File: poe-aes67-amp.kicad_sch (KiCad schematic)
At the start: 0 parts

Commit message: Setting up KiCad
Add symbols and footprints for Sheet 2 components
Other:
- added sheet Amp_Stage (sheets/amp_stage.kicad_sch)
- added sheet CM4_Carrier (sheets/cm4_carrier.kicad_sch)
- added sheet IO_Misc (sheets/io_misc.kicad_sch)
- added sheet PoE_PD (sheets/poe_pd.kicad_sch .kicad_sch)
- added sheet Power_Rails (sheets/power_rails.kicad_sch)
- company: (none) -> JCJOK3R
- title: (none) -> PoE AES67 Amplifier
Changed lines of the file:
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@@
 	(generator_version "10.0")
 	(paper "A4")
+	(title_block
+		(title "PoE AES67 Amplifier")
+		(date "2026-06-03")
+		(rev "0.1")
+		(company "JCJOK3R")
+		(comment 1 "CERN-OHL-S v2")
+	)
+	(sheet
+		(at 73.66 26.67)
+		(size 40.64 24.13)
+		(exclude_from_sim no)
+		(in_bom yes)
+		(on_board yes)
+		(dnp no)
+		(fields_autoplaced yes)
+		(stroke
+			(width 0.1524)
+			(type solid)
+		)
+		(fill
+			(color 0 0 0 0)
+		)
+		(property "Sheetname" "Power_Rails"
+			(at 73.66 25.9584 0)
+			(show_name no)
+			(do_not_autoplace no)
+			(effects
+				(font
+					(size 1.27 1.27)
+				)
+				(justify left bottom)
+			)
+		)
+		(property "Sheetfile" "sheets/power_rails.kicad_sch"
+			(at 73.66 51.3846 0)
+			(show_name no)
+			(do_not_autoplace no)
+			(effects
+				(font
+					(size 1.27 1.27)
+				)
+				(justify left top)
+			)
+		)
+		(instances
+			(project "poe-aes67-amp"
+				(path "/342711d1-e6c4-426d-85fd-6094774cf2a5"
+					(page "3")
+				)
+			)
+		)
+	)
+	(sheet
+		(at 124.46 76.2)
+		(size 38.1 24.13)
+		(exclude_from_sim no)
+		(in_bom yes)
+		(on_board yes)
+		(dnp no)
+		(fields_autoplaced yes)
+		(stroke
+			(width 0.1524)
+			(type solid)
+		)
+		(fill
+			(color 0 0 0 0)
+		)
+		(property "Sheetname" "CM4_Carrier"
+			(at 124.46 75.4884 0)
+			(show_name no)
+			(do_not_autoplace no)
+			(effects
+				(font
+					(size 1.27 1.27)
+				)
+				(justify left bottom)
+			)
+		)
+		(property "Sheetfile" "sheets/cm4_carrier.kicad_sch"
+			(at 124.46 100.9146 0)
+			(show_name no)
+			(do_not_autoplace no)
+			(effects
+				(font
+					(size 1.27 1.27)
+				)
+				(justify left top)
+			)
+		)
+		(instances
+			(project "poe-aes67-amp"
+				(path "/342711d1-e6c4-426d-85fd-6094774cf2a5"
+					(page "5")
+				)
+			)
+		)
+	)
+	(sheet
+		(at 173.99 76.2)
+		(size 34.29 24.13)
+		(exclude_from_sim no)
+		(in_bom yes)
+		(on_board yes)
+		(dnp no)
+		(fields_autoplaced yes)
+		(stroke
+			(width 0.1524)
+			(type solid)
+		)
+		(fill
+			(color 0 0 0 0)
+		)
+		(property "Sheetname" "IO_Misc"
+			(at 173.99 75.4884 0)
+			(show_name no)
+			(do_not_autoplace no)
+			(effects
+				(font
+					(size 1.27 1.27)
+				)
+				(justify left bottom)
+			)
+		)
+		(property "Sheetfile" "sheets/io_misc.kicad_sch"
+			(at 173.99 100.9146 0)
+			(show_name no)
+			(do_not_autoplace no)
+			(effects
+				(font
+					(size 1.27 1.27)
+				)
+				(justify left top)
+			)
+		)
+		(instances
+			(project "poe-aes67-amp"
+				(path "/342711d1-e6c4-426d-85fd-6094774cf2a5"
+					(page "6")
+				)
+			)
+		)
+	)
+	(sheet
+		(at 20.32 25.4)
+		(size 41.91 25.4)
+		(exclude_from_sim no)
+		(in_bom yes)
+		(on_board yes)
+		(dnp no)
+		(fields_autoplaced yes)
+		(stroke
+			(width 0.1524)
+			(type solid)
+		)
+		(fill
+			(color 0 0 0 0)
+		)
+		(property "Sheetname" "PoE_PD"
+			(at 20.32 24.6884 0)
+			(show_name no)
+			(do_not_autoplace no)
+			(effects
+				(font
+					(size 1.27 1.27)
+				)
+				(justify left bottom)
+			)
+		)
+		(property "Sheetfile" "sheets/poe_pd.kicad_sch .kicad_sch"
+			(at 20.32 51.3846 0)
+			(show_name no)
+			(do_not_autoplace no)
+			(effects
+				(font
+					(size 1.27 1.27)
+				)
+				(justify left top)
+			)
+		)
+		(instances
+			(project "poe-aes67-amp"
+				(path "/342711d1-e6c4-426d-85fd-6094774cf2a5"
+					(page "2")
+				)
+			)
+		)
+	)
+	(sheet
+		(at 124.46 27.94)
+		(size 38.1 22.86)
+		(exclude_from_sim no)
+		(in_bom yes)
+		(on_board yes)
+		(dnp no)
+		(fields_autoplaced yes)
+		(stroke
+			(width 0.1524)
+			(type solid)
+		)
+		(fill
+			(color 0 0 0 0)
+		)
+		(property "Sheetname" "Amp_Stage"
+			(at 124.46 27.2284 0)
+			(show_name no)
+			(do_not_autoplace no)
+			(effects
+				(font
+					(size 1.27 1.27)
+				)
+				(justify left bottom)
+			)
+		)
+		(property "Sheetfile" "sheets/amp_stage.kicad_sch"
+			(at 124.46 51.3846 0)
+			(show_name no)
+			(do_not_autoplace no)
+			(effects
+				(font
+					(size 1.27 1.27)
+				)
+				(justify left top)
+			)
+		)
+		(instances
+			(project "poe-aes67-amp"
+				(path "/342711d1-e6c4-426d-85fd-6094774cf2a5"
+					(page "4")
+				)
+			)
+		)
+	)
 	(sheet_instances
 		(path "/"

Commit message: Buck A config
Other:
- sheet PoE_PD ports: added BUCK_A_EN, LED_ACT, MDI1_N, MDI1_P, MDI2_N, MDI2_P, MDI3_N, MDI3_P, MDI4_N, MDI4_P; removed none
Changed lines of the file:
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@@
+			)
+		)
+		(pin "BUCK_A_EN" output
+			(at 59.69 50.8 270)
+			(effects
+				(font
+					(size 1.27 1.27)
+				)
+				(justify left)
+			)
+		)
+		(pin "LED_ACT" output
+			(at 57.15 50.8 270)
+			(effects
+				(font
+					(size 1.27 1.27)
+				)
+				(justify left)
+			)
+		)
+		(pin "MDI1_N" output
+			(at 54.61 50.8 270)
+			(effects
+				(font
+					(size 1.27 1.27)
+				)
+				(justify left)
+			)
+		)
+		(pin "MDI1_P" output
+			(at 52.07 50.8 270)
+			(effects
+				(font
+					(size 1.27 1.27)
+				)
+				(justify left)
+			)
+		)
+		(pin "MDI2_N" output
+			(at 49.53 50.8 270)
+			(effects
+				(font
+					(size 1.27 1.27)
+				)
+				(justify left)
+			)
+		)
+		(pin "MDI2_P" output
+			(at 46.99 50.8 270)
+			(effects
+				(font
+					(size 1.27 1.27)
+				)
+				(justify left)
+			)
+		)
+		(pin "MDI3_N" output
+			(at 44.45 50.8 270)
+			(effects
+				(font
+					(size 1.27 1.27)
+				)
+				(justify left)
+			)
+		)
+		(pin "MDI3_P" output
+			(at 41.91 50.8 270)
+			(effects
+				(font
+					(size 1.27 1.27)
+				)
+				(justify left)
+			)
+		)
+		(pin "MDI4_N" output
+			(at 39.37 50.8 270)
+			(effects
+				(font
+					(size 1.27 1.27)
+				)
+				(justify left)
+			)
+		)
+		(pin "MDI4_P" output
+			(at 36.83 50.8 270)
+			(effects
+				(font
+					(size 1.27 1.27)
+				)
+				(justify left)
 			)
 		)

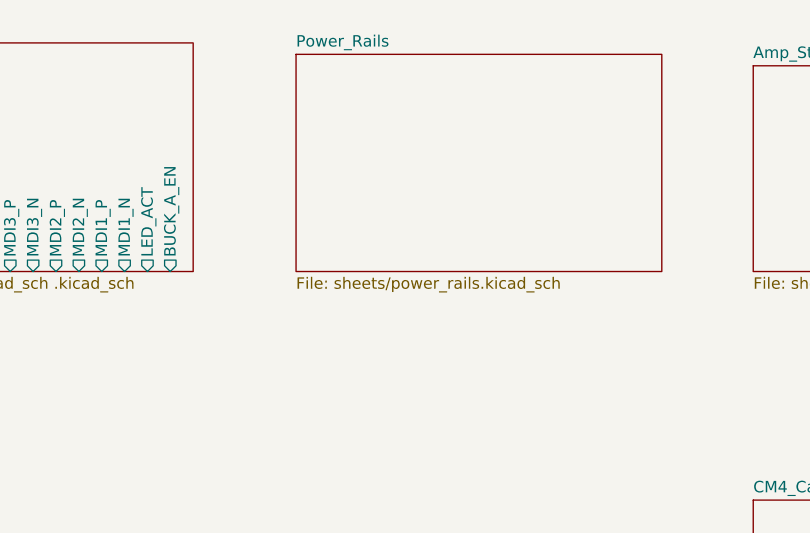
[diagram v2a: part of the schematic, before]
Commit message: Complete Sheet 4 - Amp Stage TAS3251
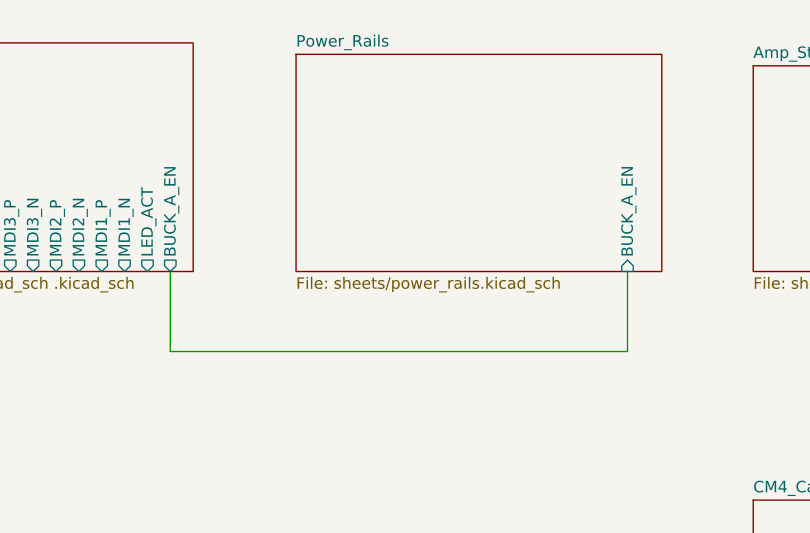
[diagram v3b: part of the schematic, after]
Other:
- sheet Power_Rails ports: added BUCK_A_EN; removed none
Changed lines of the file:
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@@
 		(comment 1 "CERN-OHL-S v2")
+	)
+	(wire
+		(pts
+			(xy 110.49 59.69) (xy 110.49 50.8)
+		)
+		(stroke
+			(width 0)
+			(type default)
+		)
+	)
+	(wire
+		(pts
+			(xy 59.69 50.8) (xy 59.69 59.69)
+		)
+		(stroke
+			(width 0)
+			(type default)
+		)
+	)
+	(wire
+		(pts
+			(xy 59.69 59.69) (xy 110.49 59.69)
+		)
+		(stroke
+			(width 0)
+			(type default)
+		)
 	)
 	(sheet
@@
 			)
 		)
+		(pin "BUCK_A_EN" input
+			(at 110.49 50.8 270)
+			(effects
+				(font
+					(size 1.27 1.27)
+				)
+				(justify left)
+			)
+		)
